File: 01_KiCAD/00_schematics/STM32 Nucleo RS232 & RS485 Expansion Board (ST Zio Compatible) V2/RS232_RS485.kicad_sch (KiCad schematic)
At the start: 38 parts, among them J1 1190299, J2 CONN D-SUB PLUG 9POS TH, J3 TCVR_PWR, U2 THVD4431RHAR

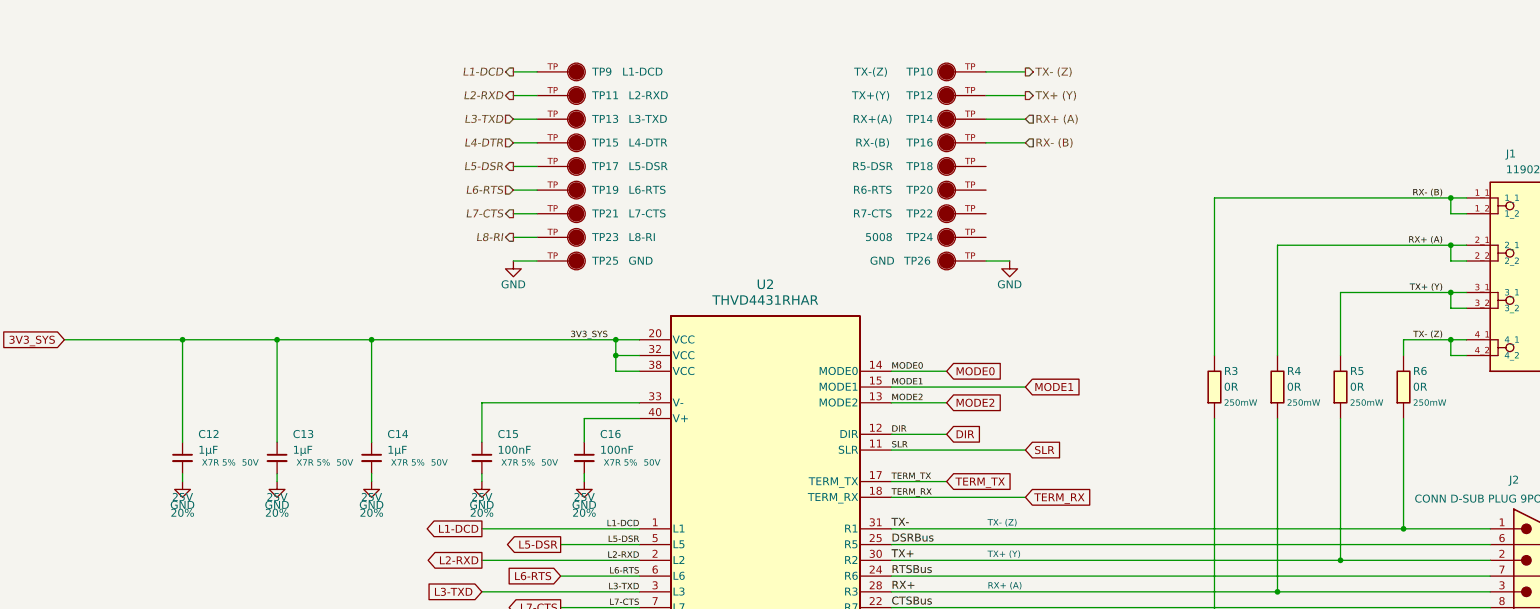
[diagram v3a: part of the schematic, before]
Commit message: Added half-duplex jumpers
Addres jumpers for hardware RS485 half-duplex configuration combining signals A(Y) & B(Z). Finalising testpoints and added 3D models for each test-point color.
-Green = logic side
-Blue = connector side
Made some minor changed to layout for test signals clarification (THVD4431 sheet)
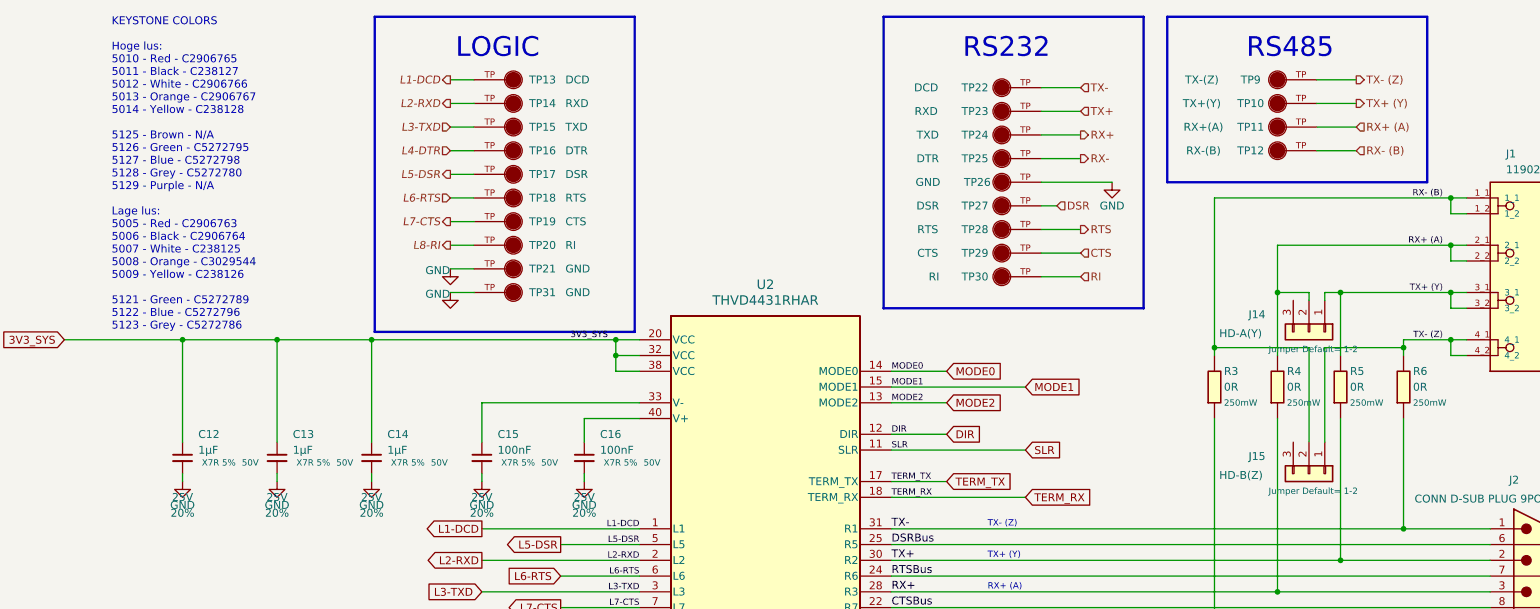
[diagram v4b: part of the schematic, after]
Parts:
- added J14: HD-A(Y), Samtec_Connector:Samtec HTSW-103-07-F-S, symbol Connector_Generic:Conn_01x03
- added J15: HD-B(Z), Samtec_Connector:Samtec HTSW-103-07-F-S, symbol Connector_Generic:Conn_01x03
- added TP22: DCD, 5009_Yellow:KEYSTONE_5009, symbol 5009_Yellow:5009
- added TP23: RXD, 5009_Yellow:KEYSTONE_5009, symbol 5009_Yellow:5009
- added TP24: TXD, 5008_Orange:KEYSTONE_5008, symbol 5008_Orange:5008
- added TP25: DTR, 5008_Orange:KEYSTONE_5008, symbol 5008_Orange:5008
- added TP31: GND, 5006_Black:KEYSTONE_5006, symbol 5006_Black:5006
- TP10: renamed from TP12; footprint 5008_Orange:KEYSTONE_5008 -> 5009_Yellow:KEYSTONE_5009; symbol 5008_Orange:5008 -> 5009_Yellow:5009; Check_prices https://www.snapeda.com/parts/5008/Keystone/view-part/?ref=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 -> https://www.snapeda.com/parts/5009/Keystone/view-part/?ref=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; Description_1 Compact THM Test Point -Orange -> Test Point Compact THM H .350 Nylon46 Insulated Yellow Phos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; MF Keystone Electronics -> Keystone Electronics Corp.; MP 5008 -> 5009; SnapEDA_Link https://www.snapeda.com/parts/5008/Keystone/view-part/?ref=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 -> https://www.snapeda.com/parts/5009/Keystone/view-part/?ref=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
- TP13: renamed from TP9; value L1-DCD -> DCD
- TP14: renamed from TP11; value L2-RXD -> RXD
- TP15: renamed from TP13; value L3-TXD -> TXD
- TP16: renamed from TP15; value L4-DTR -> DTR
- TP17: value L5-DSR -> DSR
- TP18: renamed from TP19; value L6-RTS -> RTS
- TP19: renamed from TP21; value L7-CTS -> CTS
- TP20: renamed from TP23; value L8-RI -> RI
- TP27: renamed from TP18; value R5-DSR -> DSR
- TP28: renamed from TP20; value R6-RTS -> RTS
- TP29: renamed from TP22; value R7-CTS -> CTS
- TP30: renamed from TP24; value 5008 -> RI
- TP9: renamed from TP10; footprint 5008_Orange:KEYSTONE_5008 -> 5009_Yellow:KEYSTONE_5009; symbol 5008_Orange:5008 -> 5009_Yellow:5009; Check_prices https://www.snapeda.com/parts/5008/Keystone/view-part/?ref=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 -> https://www.snapeda.com/parts/5009/Keystone/view-part/?ref=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; Description_1 Compact THM Test Point -Orange -> Test Point Compact THM H .350 Nylon46 Insulated Yellow Phos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; MF Keystone Electronics -> Keystone Electronics Corp.; MP 5008 -> 5009; SnapEDA_Link https://www.snapeda.com/parts/5008/Keystone/view-part/?ref=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 -> https://www.snapeda.com/parts/5009/Keystone/view-part/?ref=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
- renumbered TP14 to TP11, TP16 to TP12, TP25 to TP21
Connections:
- net GND: now also TP31.TP
- net RX+: now also TP24.TP
- net RX+ (A): now also J14.2 (Pin_2)
- net RX-: now also TP25.TP
- net RX- (B): now also J15.2 (Pin_2)
- net TX+: now also TP23.TP
- net TX+ (Y): now also J14.1 (Pin_1)
- net TX-: now also TP22.TP
- net TX- (Z): now also J15.1 (Pin_1)
- net CTS: now reaches TP29.TP
- net DSR: now reaches TP27.TP
- net RTS: now reaches TP28.TP
- net RI: now reaches TP30.TP
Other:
- note added: "KEYSTONE COLORS Hoge lus: 5010 - Red - C2906765 5011 - Black - C238127 5012 - White - C2906766 5013 - Orange - C2906767 5014 - Yellow - C238128 5125 - Brown - N/A 5126 - Green - C5272795 5127 - Blue - C5272798 5128 - Grey - C5272780 5129 - Purple - N/A Lage lus: 5005 - Red - C2906763 5006 - Black - C2906764 5007 - White - C238125 5008 - Orange - C3029544 5009 - Yellow - C238126 5121 - Green - C52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"
- note added: "LOGIC"
- note added: "RS232"
- note added: "RS485"
- moved on the sheet: TP10, TP11, TP12, TP13, TP14, TP15, TP16, TP17, TP18, TP19, TP20, TP21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

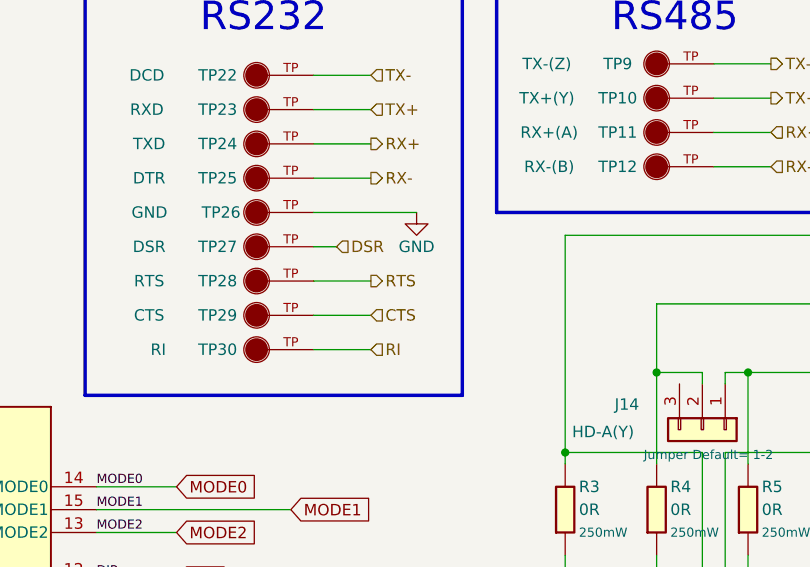
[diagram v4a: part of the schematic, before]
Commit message: Finalizing roting
Made some final routings and updated Netlist name on the schematics for some of the RS232 testpoints.
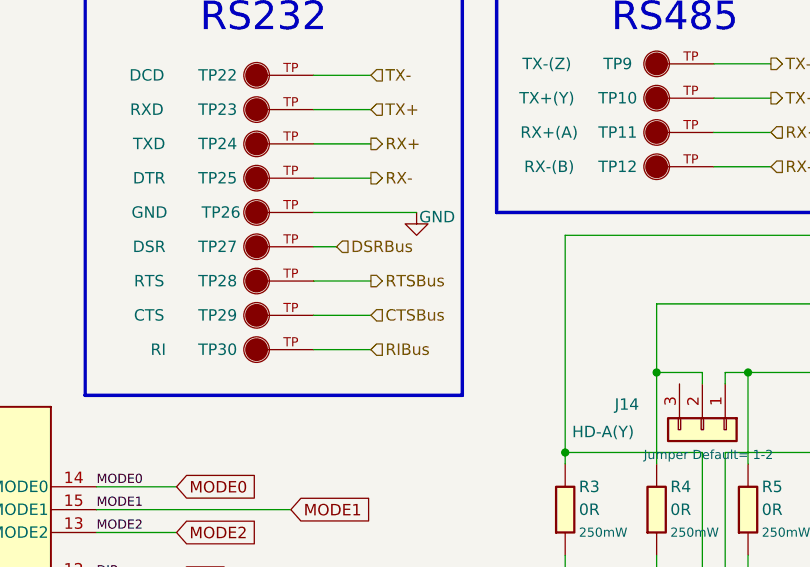
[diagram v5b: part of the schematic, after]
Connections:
- net CTS is gone; now on net CTSBus: TP29.TP
- net DSR is gone; now on net DSRBus: TP27.TP
- net RI is gone; now on net RIBus: TP30.TP
- net RTS is gone; now on net RTSBus: TP28.TP
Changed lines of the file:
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@@
 		)
 	)
-	(hierarchical_label "CTS"
+	(hierarchical_label "CTSBus"
 		(shape input)
 		(at 199.39 52.07 0)
@@
 		)
 	)
-	(hierarchical_label "RTS"
+	(hierarchical_label "RTSBus"
 		(shape output)
 		(at 199.39 48.26 0)
@@
 		)
 	)
-	(hierarchical_label "DSR"
+	(hierarchical_label "DSRBus"
 		(shape input)
 		(at 195.58 44.45 0)
@@
 		)
 	)
-	(hierarchical_label "RI"
+	(hierarchical_label "RIBus"
 		(shape input)
 		(at 199.39 55.88 0)
@@
 		(on_board yes)
 		(dnp no)
-		(fields_autoplaced yes)
 		(property "Reference" "#PWR018"
 			(at 204.47 46.99 0)
@@
 		)
 		(property "Value" "GND"
-			(at 204.47 44.45 0)
+			(at 206.756 41.148 0)
 			(do_not_autoplace yes)
 			(effects

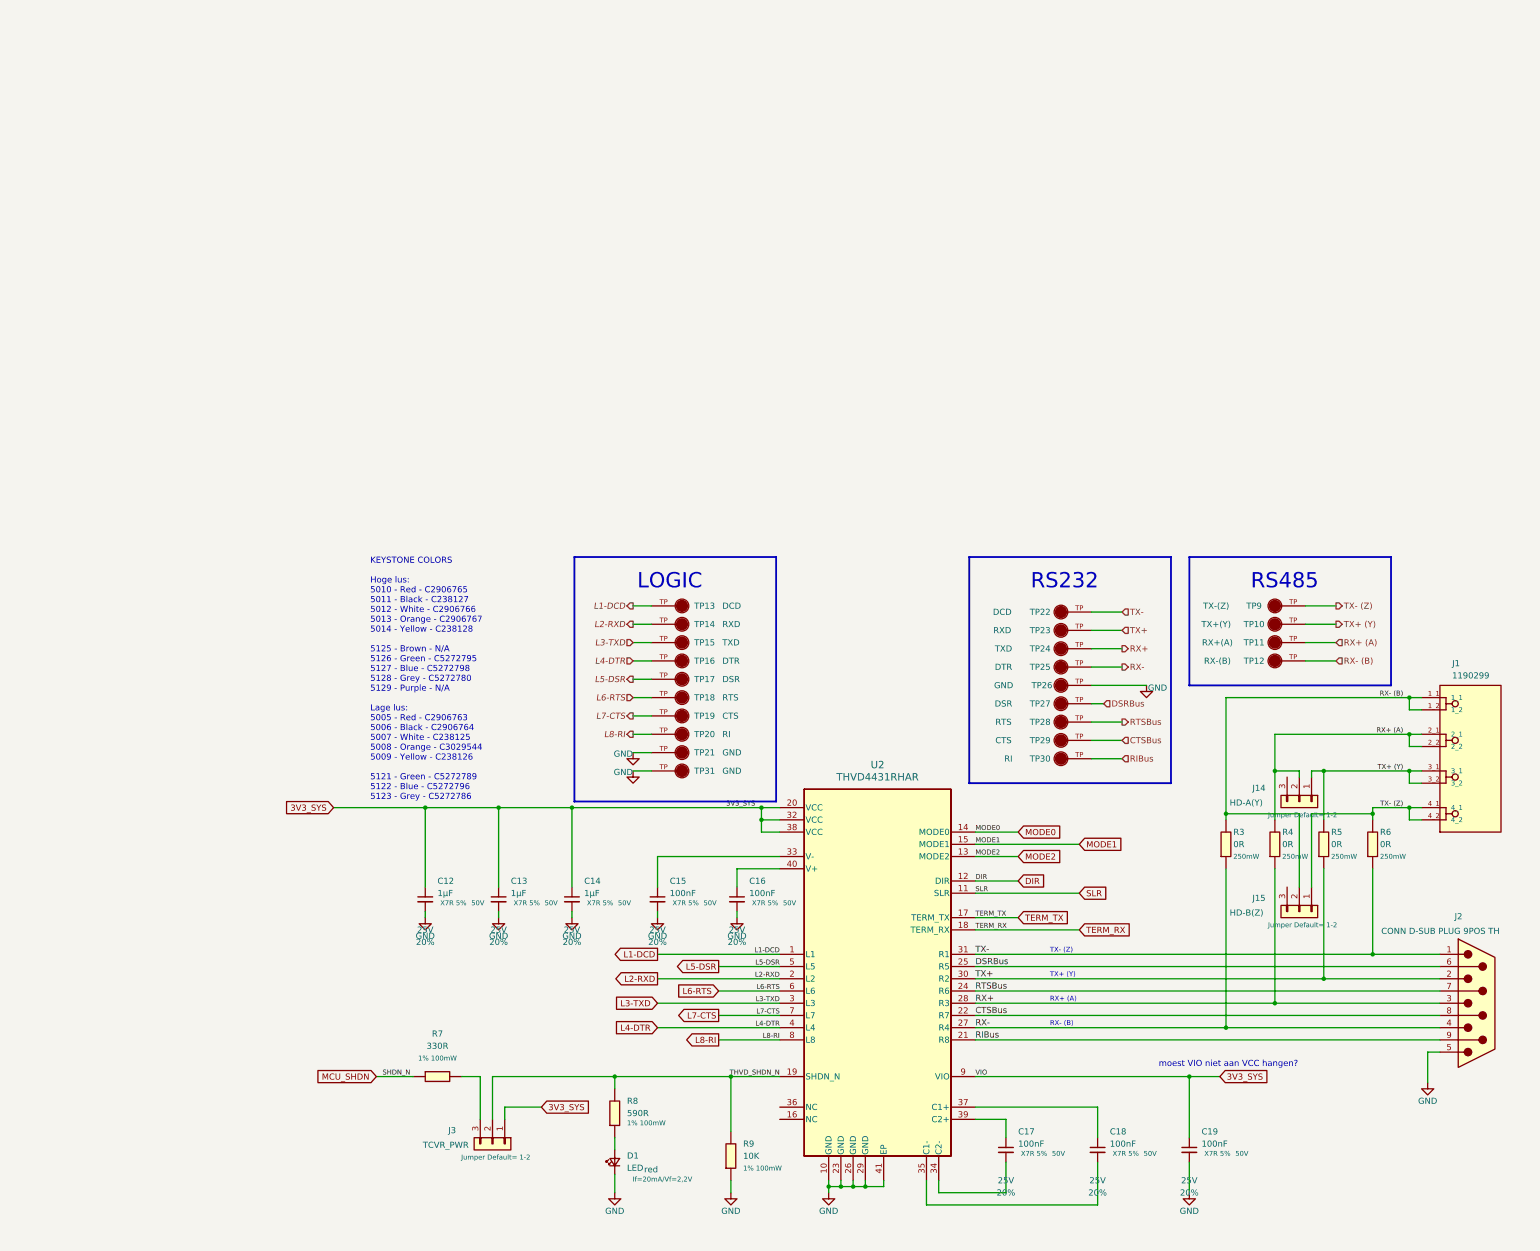
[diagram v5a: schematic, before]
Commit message: Complete redesign
Redesigned the complete board. Added hardware termination jumpers for 1120R resistors for RS485. Changes footprint, package size and simplified values between capacitors.
Still need to re-route the entire board :-(
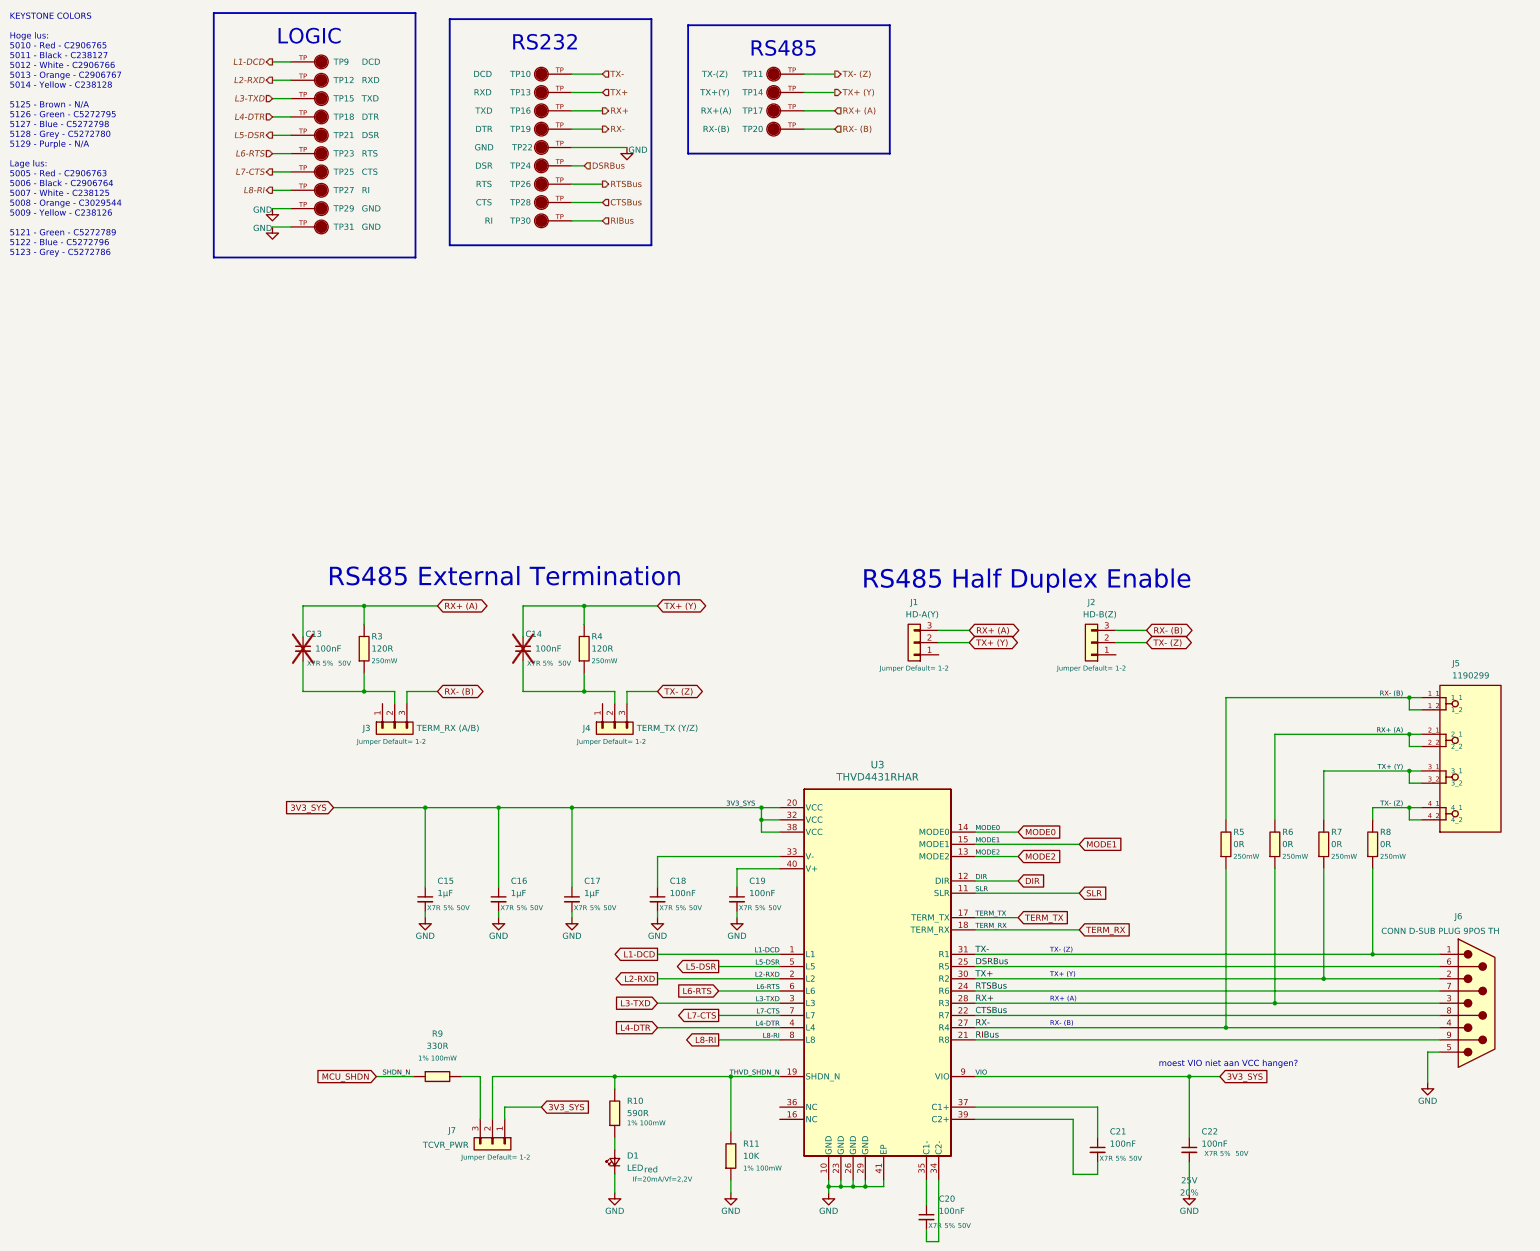
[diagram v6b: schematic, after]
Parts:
- removed C12: 1µF, PCM_SparkFun-Capacitor:C_0603_1608Metric, symbol PCM_SparkFun-Capacitor:0.1uF_0603_25V_20%
- removed C17, C18: 100nF, PCM_SparkFun-Capacitor:C_0603_1608Metric, symbol PCM_SparkFun-Capacitor:0.1uF_0603_25V_20%
- added C14: 100nF, PCM_SparkFun-Capacitor:C_0603_1608Metric, symbol PCM_SparkFun-Capacitor:0.1uF_0603_25V_20%
- added C15: 1µF, Capacitor_SMD:C_1206_3216Metric, symbol PCM_SparkFun-Capacitor:0.1uF_0603_25V_20%
- added C19, C20, C21: 100nF, Capacitor_SMD:C_0805_2012Metric, symbol PCM_SparkFun-Capacitor:0.1uF_0603_25V_20%
- added J3: TERM_RX (A/B), Samtec_Connector:Samtec HTSW-103-07-F-S, symbol Connector_Generic:Conn_01x03
- added J4: TERM_TX (Y/Z), Samtec_Connector:Samtec HTSW-103-07-F-S, symbol Connector_Generic:Conn_01x03
- added R3, R4: 120R, PCM_fab:R_0603, symbol PCM_fab:R_0603
- C13: value 1µF -> 100nF; LCSC C559769 -> C91183; MPN CC0603KRX7R9BB105 -> CC0603JRX7R9BB104; now not fitted; now left out of the parts list
- C16: value 100nF -> 1µF; footprint PCM_SparkFun-Capacitor:C_0603_1608Metric -> Capacitor_SMD:C_1206_3216Metric; Dielectric X7R 5% -> X7R; LCSC C91183 -> C597503; MPN CC0603JRX7R9BB104 -> 12065C105JAT2A; Manufacturer YAGEO -> Kyocera AVX; Package 0603 -> 1206; Tolerance 20% -> 5%; Voltage 25V -> 50V; Voltage Rating 50V -> (none)
- C17: renamed from C14; footprint PCM_SparkFun-Capacitor:C_0603_1608Metric -> Capacitor_SMD:C_1206_3216Metric; Dielectric X7R 5% -> X7R; LCSC C559769 -> C597503; MPN CC0603KRX7R9BB105 -> 12065C105JAT2A; Manufacturer YAGEO -> Kyocera AVX; Package 0603 -> 1206; Tolerance 20% -> 5%; Voltage 25V -> 50V; Voltage Rating 50V -> (none)
- C18: renamed from C15; footprint PCM_SparkFun-Capacitor:C_0603_1608Metric -> Capacitor_SMD:C_0805_2012Metric; Dielectric X7R 5% -> X7R; LCSC C91183 -> C2167095; MPN CC0603JRX7R9BB104 -> C0805C104J5RACTU; Manufacturer YAGEO -> KEMET; PROD_ID CAP-00810 -> (none); Package 0603 -> 0805; Tolerance 20% -> 5%; Voltage 25V -> 50V; Voltage Rating 50V -> (none)
- renumbered C19 to C22, J14 to J1, J15 to J2, J1 to J5, J2 to J6, J3 to J7, R8 to R10, R9 to R11, R3 to R5, R4 to R6, R5 to R7, R6 to R8, R7 to R9, TP22 to TP10, TP9 to TP11, TP14 to TP12, TP23 to TP13, TP10 to TP14, TP24 to TP16, TP11 to TP17, TP16 to TP18, TP25 to TP19, TP12 to TP20, TP17 to TP21, TP26 to TP22, TP18 to TP23, TP27 to TP24, TP19 to TP25, TP28 to TP26, TP20 to TP27, TP29 to TP28, TP21 to TP29, TP13 to TP9, U2 to U3
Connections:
- net 3V3_SYS: now also C16.1, C15.1; no longer C13.1
- net GND: now also C15.2, C19.2; no longer C13.2
- net RX+ (A): now also C13.1, J1.3 (Pin_3), R3.1; no longer J1.2 (Pin_2)
- net RX- (B): now also J2.3 (Pin_3), J3.3 (Pin_3); no longer J2.2 (Pin_2)
- net TX+ (Y): now also J1.2 (Pin_2), C14.1, R4.1; no longer J1.1 (Pin_1)
- net TX- (Z): now also J2.2 (Pin_2), J4.3 (Pin_3); no longer J2.1 (Pin_1)
- net at U3.34 (C2-): now also C20.2
- net at U3.35 (C1-): now also C20.1
- net at U3.37 (C1+): now also C21.1
- net at U3.39 (C2+): now also C21.2
- net at U3.40 (V+): now also C19.1; no longer C16.1
- new net: C14.2, J4.2 (Pin_2), R4.2
- new net: C13.2, J3.2 (Pin_2), R3.2
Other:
- note added: "RS485 External Termination"
- note added: "RS485 Half Duplex Enable"
- moved on the sheet: J1, J2, TP10, TP11, TP12, TP13, TP14, TP15, TP16, TP17, TP18, TP19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
